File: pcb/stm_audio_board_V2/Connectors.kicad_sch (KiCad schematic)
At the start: 13 parts, among them J1 Power conn, J2 STlink, J3 Audio_sig, J4 Conn_01x10_pots_internal, J5 SPI, J6 Conn_01x03_pot_ext, J6 Conn_01x03_taptempo, J8 GuitarOUT_R, J9 GuitarOUT_L

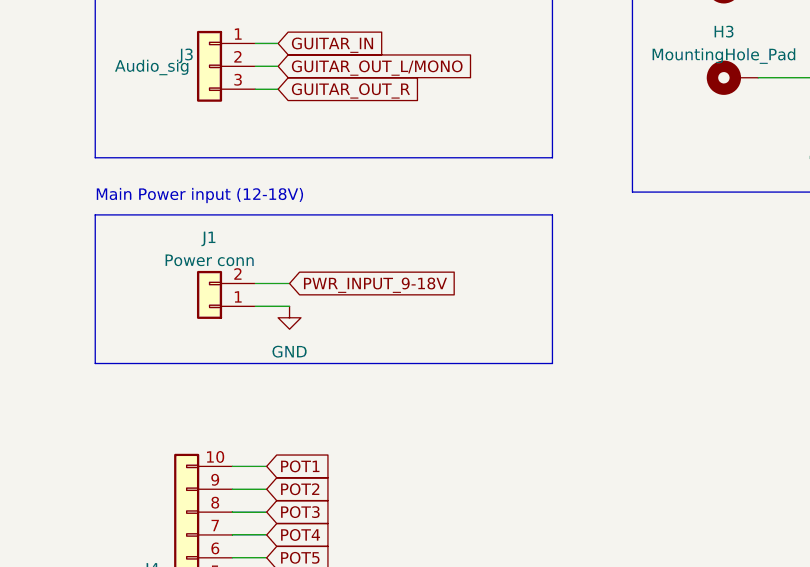
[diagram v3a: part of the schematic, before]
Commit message: PCB design started INPUT and OUTPUT stage done, codec placed
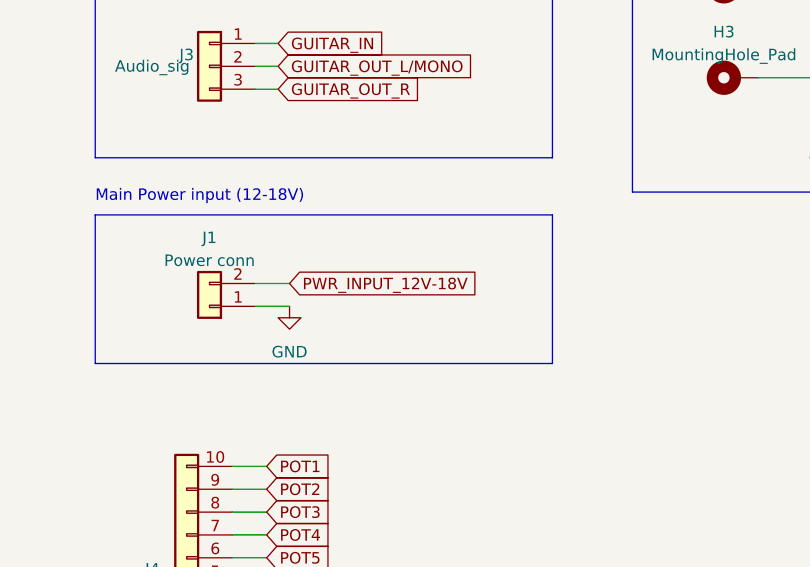
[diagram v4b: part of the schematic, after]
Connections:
- net PWR_INPUT_9-18V renamed PWR_INPUT_12V-18V
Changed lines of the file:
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@@
     )
   )
-  (global_label "PWR_INPUT_9-18V" (shape input) (at 53.34 81.28 0) (fields_autoplaced)
+  (global_label "PWR_INPUT_12V-18V" (shape input) (at 53.34 81.28 0) (fields_autoplaced)
     (effects (font (size 1.27 1.27)) (justify left))
-    (property "Intersheetrefs" "${INTERSHEET_REFS}" (at 73.9653 81.28 0)
+    (property "Intersheetrefs" "${INTERSHEET_REFS}" (at 76.2634 81.28 0)
       (effects (font (size 1.27 1.27)) (justify left) hide)
     )

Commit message: Update #auto_saved_files#, Connectors.kicad_sch, and 18 more files...
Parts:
- removed J8: GuitarOUT_R, Connector_PinHeader_2.54mm:PinHeader_1x01_P2.54mm_Vertical, symbol Connector_Generic:Conn_01x01
- removed J9: GuitarOUT_L, Connector_PinHeader_2.54mm:PinHeader_1x01_P2.54mm_Vertical, symbol Connector_Generic:Conn_01x01
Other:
- note removed: "These are for debug reasons"
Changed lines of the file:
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@@
-    (stroke (width 0) (type default))
-  )
-  (wire (pts (xy 46.99 39.37) (xy 52.07 39.37))
     (stroke (width 0) (type default))
   )
@@
     (stroke (width 0) (type default))
   )
-  (wire (pts (xy 46.99 30.48) (xy 53.34 30.48))
-    (stroke (width 0) (type default))
-  )
   (wire (pts (xy 49.53 81.28) (xy 53.34 81.28))
     (stroke (width 0) (type default))
@@
   )
   (rectangle (start 31.75 73.66) (end 82.55 90.17)
-    (stroke (width 0) (type default))
-    (fill (type none))
-  )
-  (rectangle (start 31.75 24.13) (end 82.55 41.91)
     (stroke (width 0) (type default))
     (fill (type none))
@@
   )
   (text "Guitar signals I/O" (at 31.75 48.26 0)
-    (effects (font (size 1.27 1.27)) (justify left bottom))
-  )
-  (text "These are for debug reasons\n" (at 30.48 22.86 0)
     (effects (font (size 1.27 1.27)) (justify left bottom))
   )
@@
     )
   )
-  (global_label "audio_OUT_R" (shape input) (at 53.34 30.48 0) (fields_autoplaced)
-    (effects (font (size 1.27 1.27)) (justify left))
-    (property "Intersheetrefs" "${INTERSHEET_REFS}" (at 68.2804 30.48 0)
-      (effects (font (size 1.27 1.27)) (justify left) hide)
-    )
-  )
   (global_label "MOSI" (shape input) (at 119.38 100.33 180) (fields_autoplaced)
     (effects (font (size 1.27 1.27)) (justify right))
@@
     )
   )
-  (global_label "audio_OUT_L{slash}MONO" (shape input) (at 52.07 39.37 0) (fields_autoplaced)
-    (effects (font (size 1.27 1.27)) (justify left))
-    (property "Intersheetrefs" "${INTERSHEET_REFS}" (at 73.5419 39.37 0)
-      (effects (font (size 1.27 1.27)) (justify left) hide)
-    )
-  )
   (global_label "POT4" (shape input) (at 50.8 109.22 0) (fields_autoplaced)
     (effects (font (size 1.27 1.27)) (justify left))
@@
         (path "/6997cf63-2615-4e49-9471-e7da1b6bae71/6424856c-1346-4018-a943-0d16008c9545"
           (reference "H3") (unit 1)
-        )
-      )
-    )
-  )
-  (symbol (lib_id "Connector_Generic:Conn_01x01") (at 41.91 30.48 180) (unit 1)
-    (in_bom yes) (on_board yes) (dnp no) (fields_autoplaced)
-    (property "Reference" "J8" (at 41.91 25.4 0)
-      (effects (font (size 1.27 1.27)))
-    )
-    (property "Value" "GuitarOUT_R" (at 41.91 27.94 0)
-      (effects (font (size 1.27 1.27)))
-    )
-    (property "Footprint" "Connector_PinHeader_2.54mm:PinHeader_1x01_P2.54mm_Vertical" (at 41.91 30.48 0)
-      (effects (font (size 1.27 1.27)) hide)
-    )
-    (property "Datasheet" "~" (at 41.91 30.48 0)
-      (effects (font (size 1.27 1.27)) hide)
-    )
-    (pin "1")
-    (instances
-      (project "stm_audio_board_V2"
-        (path "/6997cf63-2615-4e49-9471-e7da1b6bae71"
-          (reference "J8") (unit 1)
-        )
-        (path "/6997cf63-2615-4e49-9471-e7da1b6bae71/83920463-7bb1-4088-aad8-702bcdea14ea"
-          (reference "J8") (unit 1)
-        )
-        (path "/6997cf63-2615-4e49-9471-e7da1b6bae71/6424856c-1346-4018-a943-0d16008c9545"
-          (reference "J8") (unit 1)
         )
       )
@@
         )
       )
-    )
-  )
-  (symbol (lib_id "Connector_Generic:Conn_01x01") (at 41.91 39.37 180) (unit 1)
-    (in_bom yes) (on_board yes) (dnp no) (fields_autoplaced)
-    (property "Reference" "J9" (at 41.91 34.29 0)
-      (effects (font (size 1.27 1.27)))
-    )
-    (property "Value" "GuitarOUT_L" (at 41.91 36.83 0)
-      (effects (font (size 1.27 1.27)))
-    )
-    (property "Footprint" "Connector_PinHeader_2.54mm:PinHeader_1x01_P2.54mm_Vertical" (at 41.91 39.37 0)
-      (effects (font (size 1.27 1.27)) hide)
-    )
-    (property "Datasheet" "~" (at 41.91 39.37 0)
-      (effects (font (size 1.27 1.27)) hide)
-    )
-    (pin "1")
-    (instances
-      (project "stm_audio_board_V2"
-        (path "/6997cf63-2615-4e49-9471-e7da1b6bae71"
-          (reference "J9") (unit 1)
-        )
-        (path "/6997cf63-2615-4e49-9471-e7da1b6bae71/83920463-7bb1-4088-aad8-702bcdea14ea"
-          (reference "J9") (unit 1)
-        )
-        (path "/6997cf63-2615-4e49-9471-e7da1b6bae71/6424856c-1346-4018-a943-0d16008c9545"
-          (reference "J9") (unit 1)
-        )
-      )

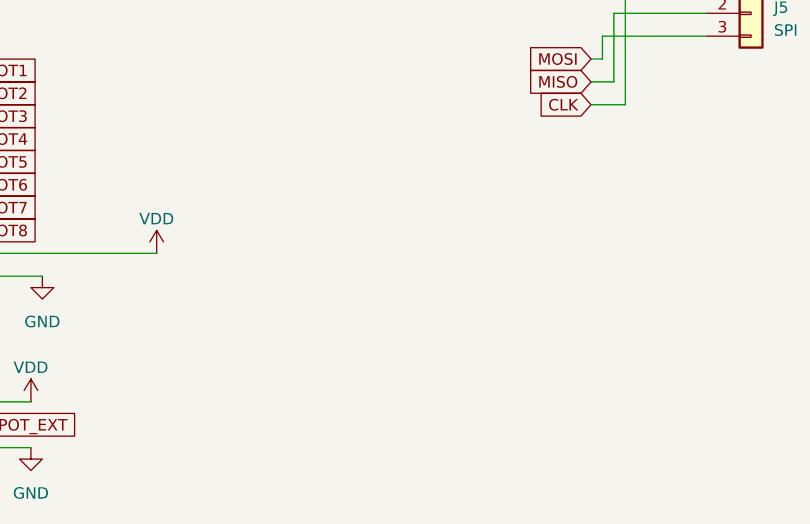
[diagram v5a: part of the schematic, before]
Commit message: pinout added, pcb is updated according to pinout excel
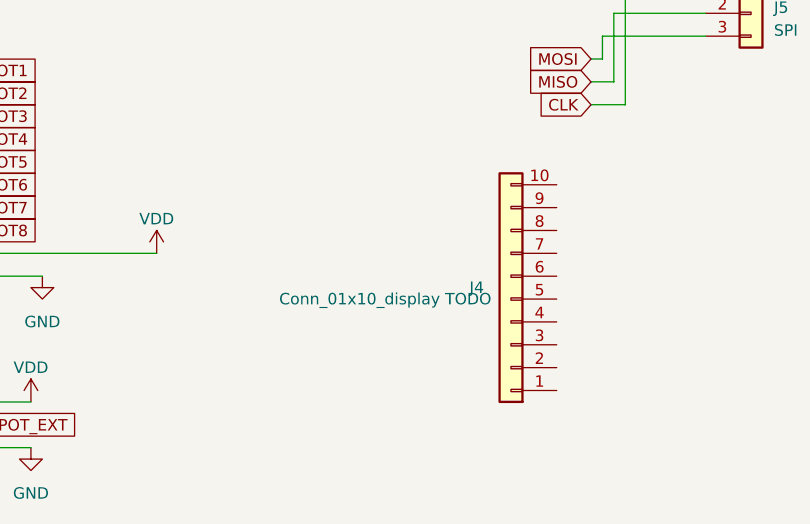
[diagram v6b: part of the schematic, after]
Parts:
- added J4: Conn_01x10_display TODO, Connector_PinHeader_2.54mm:PinHeader_1x10_P2.54mm_Vertical, symbol Connector_Generic:Conn_01x10
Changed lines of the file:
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@@
+    )
+  )
+  (symbol (lib_id "Connector_Generic:Conn_01x10") (at 110.49 127 180) (unit 1)
+    (in_bom yes) (on_board yes) (dnp no)
+    (property "Reference" "J4" (at 106.68 125.73 0)
+      (effects (font (size 1.27 1.27)))
+    )
+    (property "Value" "Conn_01x10_display TODO" (at 96.52 127 0)
+      (effects (font (size 1.27 1.27)))
+    )
+    (property "Footprint" "Connector_PinHeader_2.54mm:PinHeader_1x10_P2.54mm_Vertical" (at 110.49 127 0)
+      (effects (font (size 1.27 1.27)) hide)
+    )
+    (property "Datasheet" "~" (at 110.49 127 0)
+      (effects (font (size 1.27 1.27)) hide)
+    )
+    (pin "1")
+    (pin "10")
+    (pin "2")
+    (pin "3")
+    (pin "4")
+    (pin "5")
+    (pin "6")
+    (pin "7")
+    (pin "8")
+    (pin "9")
+    (instances
+      (project "stm_audio_board_V2"
+        (path "/6997cf63-2615-4e49-9471-e7da1b6bae71"
+          (reference "J4") (unit 1)
+        )
+        (path "/6997cf63-2615-4e49-9471-e7da1b6bae71/6424856c-1346-4018-a943-0d16008c9545"
+          (reference "J5") (unit 1)
+        )
+      )
     )
   )

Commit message: pinsetup ready
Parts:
- J4: value Conn_01x10_display TODO -> Conn_01x10_display
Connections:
- net GND: now also J4.2 (Pin_2)
- net VDD: now also J4.1 (Pin_1)
- net TOUCH_IRQ: now reaches J4.10 (Pin_10)
- net DISPLAY_CS: now reaches J4.3 (Pin_3)
- net DISPLAY_RST: now reaches J4.4 (Pin_4)
- net DISPLAY_DC: now reaches J4.5 (Pin_5)
- net DISPLAY_MOSI: now reaches J4.6 (Pin_6)
- net DISPLAY_SCK: now reaches J4.7 (Pin_7)
- net DISPLAY_MISO: now reaches J4.8 (Pin_8)
- net TOUCH_CS: now reaches J4.9 (Pin_9)
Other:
- moved on the sheet: J4
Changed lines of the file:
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@@
+    (stroke (width 0) (type default))
+  )
+  (wire (pts (xy 119.38 132.08) (xy 121.92 132.08))
     (stroke (width 0) (type default))
   )
@@
     (stroke (width 0) (type default))
   )
+  (wire (pts (xy 119.38 134.62) (xy 121.92 134.62))
+    (stroke (width 0) (type default))
+  )
   (wire (pts (xy 48.26 143.51) (xy 57.15 143.51))
     (stroke (width 0) (type default))
@@
     (stroke (width 0) (type default))
   )
+  (wire (pts (xy 119.38 127) (xy 121.92 127))
+    (stroke (width 0) (type default))
+  )
+  (wire (pts (xy 119.38 137.16) (xy 121.92 137.16))
+    (stroke (width 0) (type default))
+  )
   (wire (pts (xy 46.99 101.6) (xy 50.8 101.6))
     (stroke (width 0) (type default))
@@
     (stroke (width 0) (type default))
   )
+  (wire (pts (xy 119.38 139.7) (xy 121.92 139.7))
+    (stroke (width 0) (type default))
+  )
+  (wire (pts (xy 105.41 119.38) (xy 121.92 119.38))
+    (stroke (width 0) (type default))
+  )
+  (wire (pts (xy 119.38 124.46) (xy 121.92 124.46))
+    (stroke (width 0) (type default))
+  )
   (wire (pts (xy 146.05 40.64) (xy 142.24 40.64))
     (stroke (width 0) (type default))
@@
     (stroke (width 0) (type default))
   )
+  (wire (pts (xy 99.06 121.92) (xy 121.92 121.92))
+    (stroke (width 0) (type default))
+  )
   (wire (pts (xy 105.41 39.37) (xy 113.03 39.37))
     (stroke (width 0) (type default))
@@
     (stroke (width 0) (type default))
   )
+  (wire (pts (xy 119.38 142.24) (xy 121.92 142.24))
+    (stroke (width 0) (type default))
+  )
   (wire (pts (xy 142.24 35.56) (xy 146.05 35.56))
     (stroke (width 0) (type default))
@@
   )
   (wire (pts (xy 46.99 106.68) (xy 50.8 106.68))
+    (stroke (width 0) (type default))
+  )
+  (wire (pts (xy 119.38 129.54) (xy 121.92 129.54))
     (stroke (width 0) (type default))
   )
@@
     (effects (font (size 1.27 1.27)) (justify left bottom))
   )
+  (global_label "DISPLAY_DC" (shape input) (at 119.38 129.54 180) (fields_autoplaced)
+    (effects (font (size 1.27 1.27)) (justify right))
+    (property "Intersheetrefs" "${INTERSHEET_REFS}" (at 105.407 129.54 0)
+      (effects (font (size 1.27 1.27)) (justify right) hide)
+    )
+  )
   (global_label "POT3" (shape input) (at 50.8 106.68 0) (fields_autoplaced)
     (effects (font (size 1.27 1.27)) (justify left))
@@
     )
   )
+  (global_label "DISPLAY_RST" (shape input) (at 119.38 127 180) (fields_autoplaced)
+    (effects (font (size 1.27 1.27)) (justify right))
+    (property "Intersheetrefs" "${INTERSHEET_REFS}" (at 104.4999 127 0)
+      (effects (font (size 1.27 1.27)) (justify right) hide)
+    )
+  )
   (global_label "POT7" (shape input) (at 50.8 116.84 0) (fields_autoplaced)
     (effects (font (size 1.27 1.27)) (justify left))
@@
     )
   )
+  (global_label "TOUCH_CS" (shape input) (at 119.38 139.7 180) (fields_autoplaced)
+    (effects (font (size 1.27 1.27)) (justify right))
+    (property "Intersheetrefs" "${INTERSHEET_REFS}" (at 106.798 139.7 0)
+      (effects (font (size 1.27 1.27)) (justify right) hide)
+    )
+  )
   (global_label "TAP_TEMPO_INPUT" (shape input) (at 158.75 68.58 0) (fields_autoplaced)
     (effects (font (size 1.27 1.27)) (justify left))
@@
     )
   )
+  (global_label "DISPLAY_SCK" (shape input) (at 119.38 134.62 180) (fields_autoplaced)
+    (effects (font (size 1.27 1.27)) (justify right))
+    (property "Intersheetrefs" "${INTERSHEET_REFS}" (at 104.1975 134.62 0)
+      (effects (font (size 1.27 1.27)) (justify right) hide)
+    )
+  )
   (global_label "SWCLK" (shape input) (at 146.05 35.56 0) (fields_autoplaced)
     (effects (font (size 1.27 1.27)) (justify left))
@@
     )
   )
+  (global_label "DISPLAY_CS" (shape input) (at 119.38 124.46 180) (fields_autoplaced)
+    (effects (font (size 1.27 1.27)) (justify right))
+    (property "Intersheetrefs" "${INTERSHEET_REFS}" (at 105.4675 124.46 0)
+      (effects (font (size 1.27 1.27)) (justify right) hide)
+    )
+  )
   (global_label "POT8" (shape input) (at 50.8 119.38 0) (fields_autoplaced)
     (effects (font (size 1.27 1.27)) (justify left))
@@
     )
   )
+  (global_label "TOUCH_IRQ" (shape input) (at 119.38 142.24 180) (fields_autoplaced)
+    (effects (font (size 1.27 1.27)) (justify right))
+    (property "Intersheetrefs" "${INTERSHEET_REFS}" (at 106.0722 142.24 0)
+      (effects (font (size 1.27 1.27)) (justify right) hide)
+    )
+  )
   (global_label "MOSI" (shape input) (at 119.38 100.33 180) (fields_autoplaced)
     (effects (font (size 1.27 1.27)) (justify right))
@@
     )
   )
+  (global_label "DISPLAY_MOSI" (shape input) (at 119.38 132.08 180) (fields_autoplaced)
+    (effects (font (size 1.27 1.27)) (justify right))
+    (property "Intersheetrefs" "${INTERSHEET_REFS}" (at 103.3508 132.08 0)
+      (effects (font (size 1.27 1.27)) (justify right) hide)
+    )
+  )
   (global_label "POT2" (shape input) (at 50.8 104.14 0) (fields_autoplaced)
     (effects (font (size 1.27 1.27)) (justify left))
@@
     (property "Intersheetrefs" "${INTERSHEET_REFS}" (at 76.2634 81.28 0)
       (effects (font (size 1.27 1.27)) (justify left) hide)
+    )
+  )
+  (global_label "DISPLAY_MISO" (shape input) (at 119.38 137.16 180) (fields_autoplaced)
+    (effects (font (size 1.27 1.27)) (justify right))
+    (property "Intersheetrefs" "${INTERSHEET_REFS}" (at 103.3508 137.16 0)
+      (effects (font (size 1.27 1.27)) (justify right) hide)
     )
   )
@@
     )
   )
+  (symbol (lib_id "power:GND") (at 99.06 121.92 0) (unit 1)
+    (in_bom yes) (on_board yes) (dnp no) (fields_autoplaced)
+    (property "Reference" "#PWR052" (at 99.06 128.27 0)
+      (effects (font (size 1.27 1.27)) hide)
+    )
+    (property "Value" "GND" (at 99.06 127 0)
+      (effects (font (size 1.27 1.27)))
+    )
+    (property "Footprint" "" (at 99.06 121.92 0)
+      (effects (font (size 1.27 1.27)) hide)
+    )
+    (property "Datasheet" "" (at 99.06 121.92 0)
+      (effects (font (size 1.27 1.27)) hide)
+    )
+    (pin "1")
+    (instances
+      (project "stm_audio_board_V2"
+        (path "/6997cf63-2615-4e49-9471-e7da1b6bae71"
+          (reference "#PWR052") (unit 1)
+        )
+        (path "/6997cf63-2615-4e49-9471-e7da1b6bae71/6424856c-1346-4018-a943-0d16008c9545"
+          (reference "#PWR095") (unit 1)
+        )
+      )
+    )
+  )
   (symbol (lib_id "power:GND") (at 146.05 41.91 0) (unit 1)
     (in_bom yes) (on_board yes) (dnp no) (fields_autoplaced)
@@
     )
   )
-  (symbol (lib_id "Connector_Generic:Conn_01x10") (at 110.49 127 180) (unit 1)
+  (symbol (lib_id "Connector_Generic:Conn_01x10") (at 127 129.54 0) (unit 1)
     (in_bom yes) (on_board yes) (dnp no)
-    (property "Reference" "J4" (at 106.68 125.73 0)
-      (effects (font (size 1.27 1.27)))
-    )
-    (property "Value" "Conn_01x10_display TODO" (at 96.52 127 0)
-      (effects (font (size 1.27 1.27)))
-    )
-    (property "Footprint" "Connector_PinHeader_2.54mm:PinHeader_1x10_P2.54mm_Vertical" (at 110.49 127 0)
-      (effects (font (size 1.27 1.27)) hide)
-    )
-    (property "Datasheet" "~" (at 110.49 127 0)
+    (property "Reference" "J4" (at 130.81 130.81 0)
+      (effects (font (size 1.27 1.27)))
+    )
+    (property "Value" "Conn_01x10_display" (at 138.43 133.35 0)
+      (effects (font (size 1.27 1.27)))
+    )
+    (property "Footprint" "Connector_PinHeader_2.54mm:PinHeader_1x10_P2.54mm_Vertical" (at 127 129.54 0)
+      (effects (font (size 1.27 1.27)) hide)
+    )
+    (property "Datasheet" "~" (at 127 129.54 0)
       (effects (font (size 1.27 1.27)) hide)
     )
@@
         )
       )
+    )
+  )
+  (symbol (lib_id "power:VDD") (at 105.41 119.38 0) (unit 1)
+    (in_bom yes) (on_board yes) (dnp no) (fields_autoplaced)
+    (property "Reference" "#PWR051" (at 105.41 123.19 0)
+      (effects (font (size 1.27 1.27)) hide)
+    )
+    (property "Value" "VDD" (at 105.41 115.57 0)
+      (effects (font (size 1.27 1.27)))
+    )
+    (property "Footprint" "" (at 105.41 119.38 0)
+      (effects (font (size 1.27 1.27)) hide)
+    )
+    (property "Datasheet" "" (at 105.41 119.38 0)
+      (effects (font (size 1.27 1.27)) hide)
+    )
+    (pin "1")
+    (instances
+      (project "stm_audio_board_V2"
+        (path "/6997cf63-2615-4e49-9471-e7da1b6bae71"
+          (reference "#PWR051") (unit 1)
+        )
+        (path "/6997cf63-2615-4e49-9471-e7da1b6bae71/6424856c-1346-4018-a943-0d16008c9545"
+          (reference "#PWR036") (unit 1)
+        )
+      )
